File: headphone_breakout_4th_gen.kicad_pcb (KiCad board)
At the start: 2 copper layers, 26.7 x 27.9 mm, 4 parts, among them J1 AudioPlug4, J2 Conn_01x04, J3 AudioJack4, J4 Conn_01x04

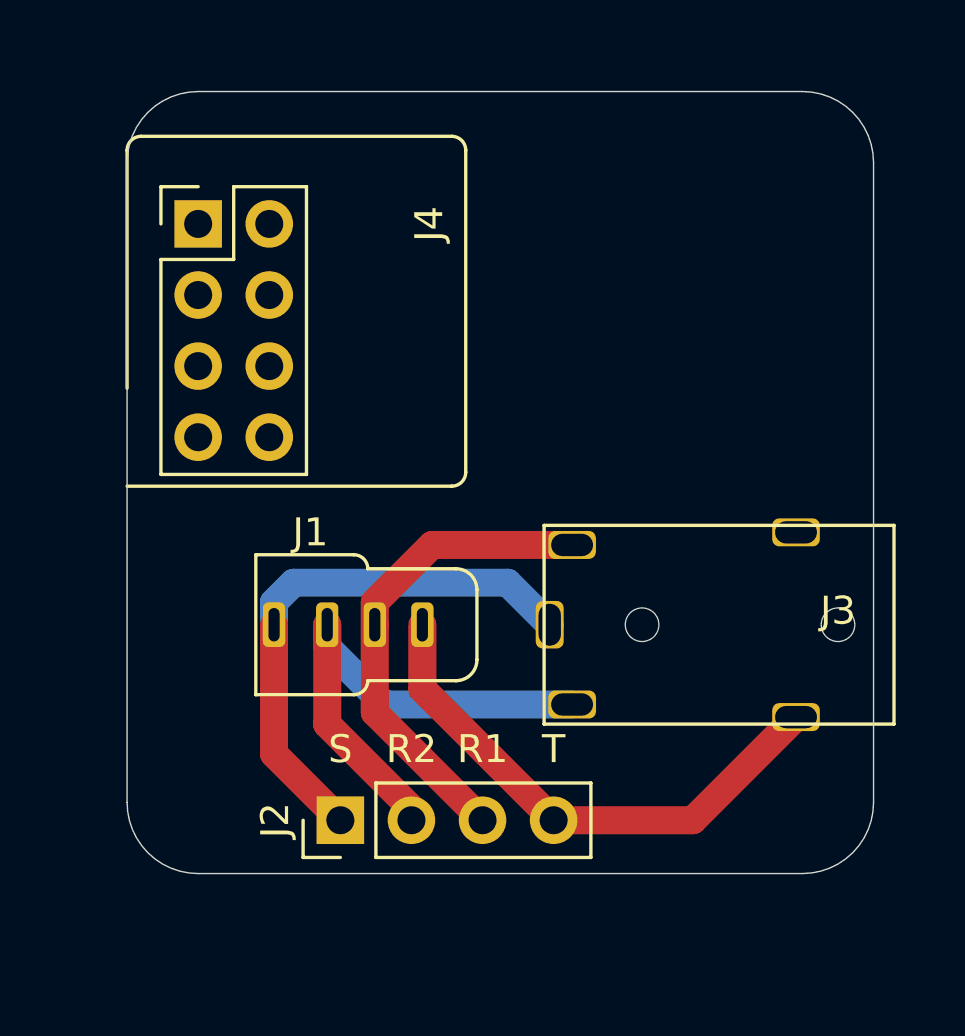
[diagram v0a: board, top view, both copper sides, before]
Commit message: Fill unused areas with copper, update remote connector with connector pads
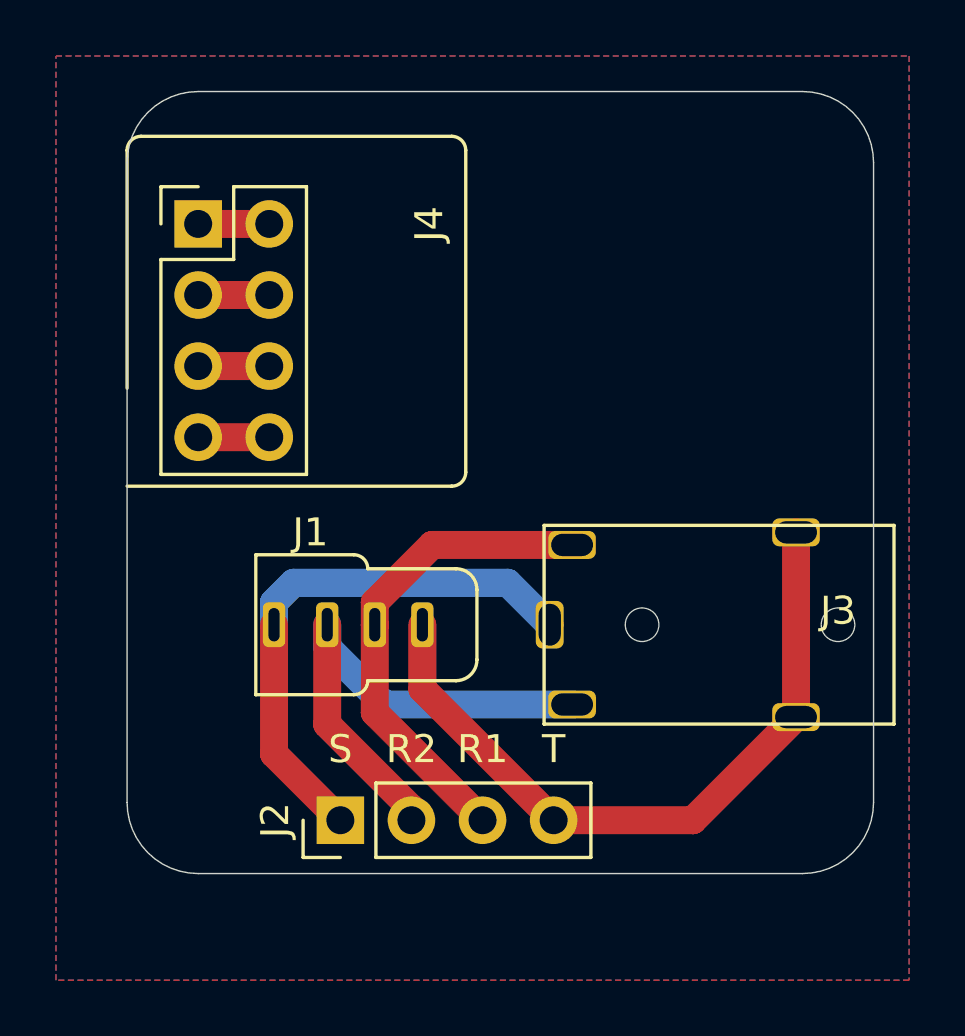
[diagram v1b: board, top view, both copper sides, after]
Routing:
- net /TIP: track 19.1 -> 25.7 mm
- net Net-(J4-Pad4): track 0.00 -> 2.54 mm
- net Net-(J4-Pad3): track 0.00 -> 2.54 mm
- net Net-(J4-Pad2): track 0.00 -> 2.54 mm
- net Net-(J4-Pad1): track 0.00 -> 2.54 mm
- added copper zone on B.Cu, net (none)
- added copper zone on F.Cu, net (none)

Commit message: Prepare for JLCPCB
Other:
- board text added: "JLCJLCJLCJLC"
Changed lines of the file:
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@@
   (general
     (thickness 1.6)
-    (drawings 13)
+    (drawings 14)
     (tracks 26)
     (zones 0)
@@
   )
   (setup
-    (last_trace_width 1)
+    (last_trace_width 0.25)
     (user_trace_width 1)
     (trace_clearance 0.2)
@@
       (outputformat 1)
       (mirror false)
-      (drillshape 1)
+      (drillshape 0)
       (scaleselection 1)
-      (outputdirectory ""))
+      (outputdirectory "export_headphone/"))
   )
   (net 0 "")
@@
   (module Gigahawk:IPOD_4TH_REMOTE_BREAKOUT (layer F.Cu)
     (at 0 -6.7 270)
-    (fp_text reference J4 (at -7.62 -10.795 90) (layer F.SilkS)
+    (fp_text reference J4 (at -9.175 -13.335 90) (layer F.SilkS)
       (effects (font (size 1 1) (thickness 0.15)))
     )
@@
   (module Gigahawk:54-00174 (layer F.Cu)
     (at 25.4 0 180)
-    (fp_text reference J3 (at 0 0.5) (layer F.SilkS)
+    (fp_text reference J3 (at 5.715 4.445) (layer F.SilkS)
       (effects (font (size 1 1) (thickness 0.15)))
     )
@@
     )
   )
+  (gr_text JLCJLCJLCJLC (at 8.89 -10.795 270) (layer F.SilkS)
+    (effects (font (size 0.8 0.8) (thickness 0.15)))
+  )
   (gr_arc (start 2.54 6.35) (end 0 6.35) (angle -90) (layer Edge.Cuts) (width 0.05))

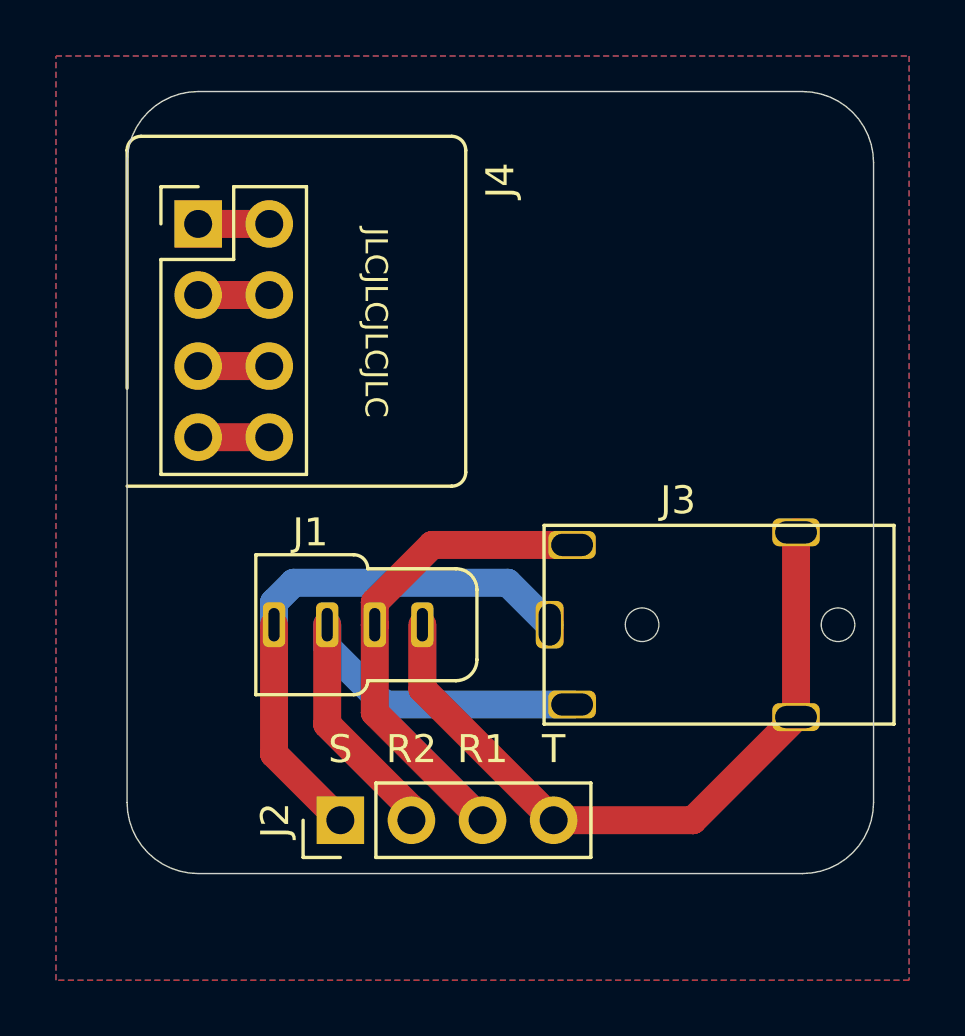
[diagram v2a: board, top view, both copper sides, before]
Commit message: Add labels for remote connector
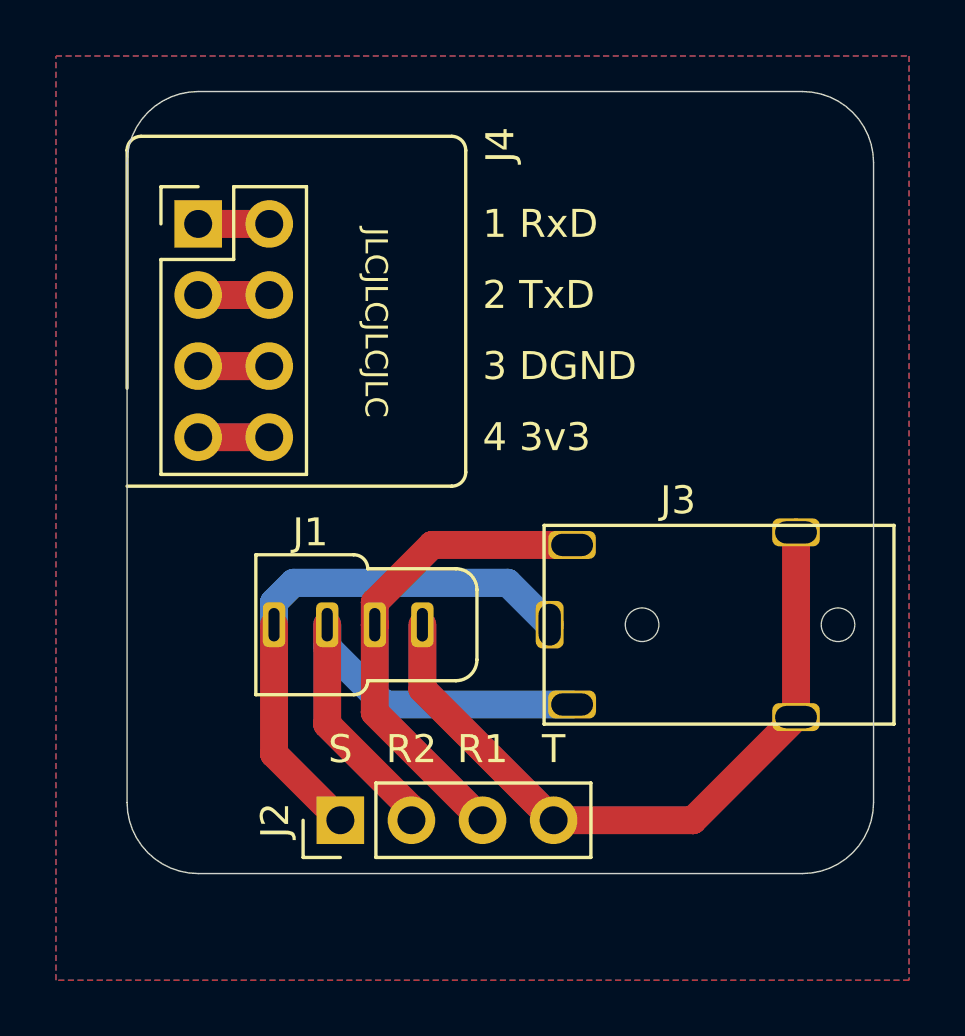
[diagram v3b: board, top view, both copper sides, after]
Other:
- board text added: "1 RxD"
- board text added: "2 TxD"
- board text added: "3 DGND"
- board text added: "4 3v3"
